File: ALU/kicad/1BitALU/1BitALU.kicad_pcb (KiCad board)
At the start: 2 copper layers, 171.5 x 123.2 mm, 55 parts, among them P1 CONN_6, P2 CONN_2, P3 Power, U1 xor3a, U10 and3a, U11 or2a, U12 and3b, U13 inv3b, U14 and3c, U15 or3a, U16 xor1b, U17 xor1a, U18 xor2b, U19 and4a, U2 and2a, U20 xor2a, U21 and4b, U22 and4c, U23 or3b, U24 and5a, U25 and5b, U26 inv5c, U27 and5c, U28 or3c, U29 and6a, U3 xor3b, U30 inv6b, U31 and6b, U32 inv6c, U33 and6c, U34 or3d, U4 and2b, U5 or1b, U6 and1a, U7 and1b, U8 or1a, U9 or2b

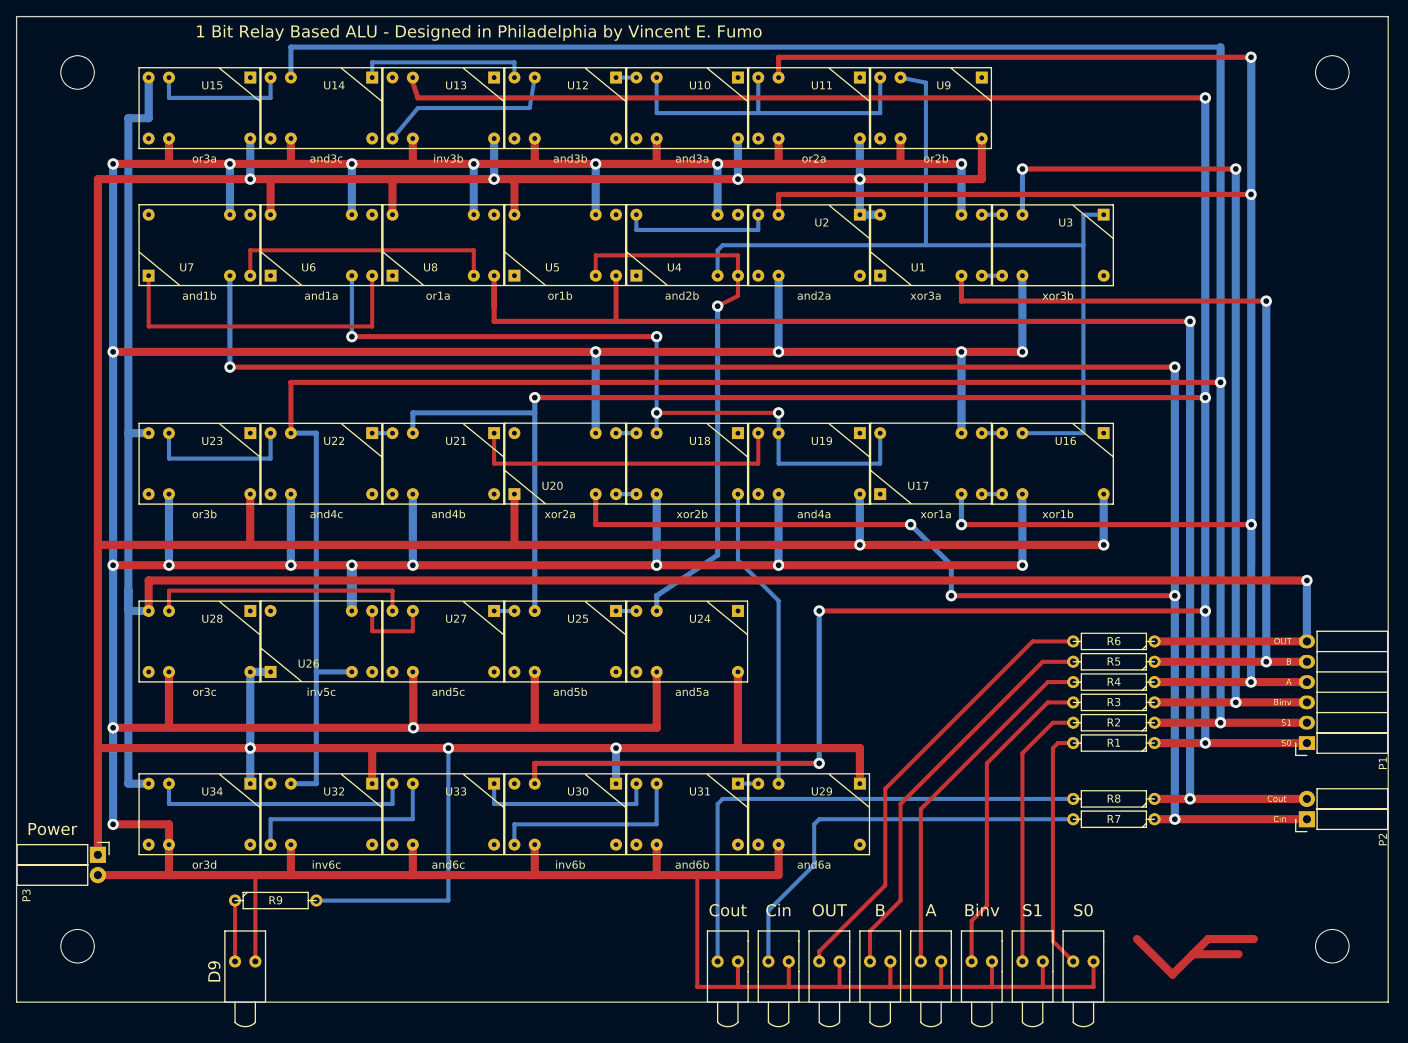
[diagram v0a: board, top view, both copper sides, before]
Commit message: bigger drill holes
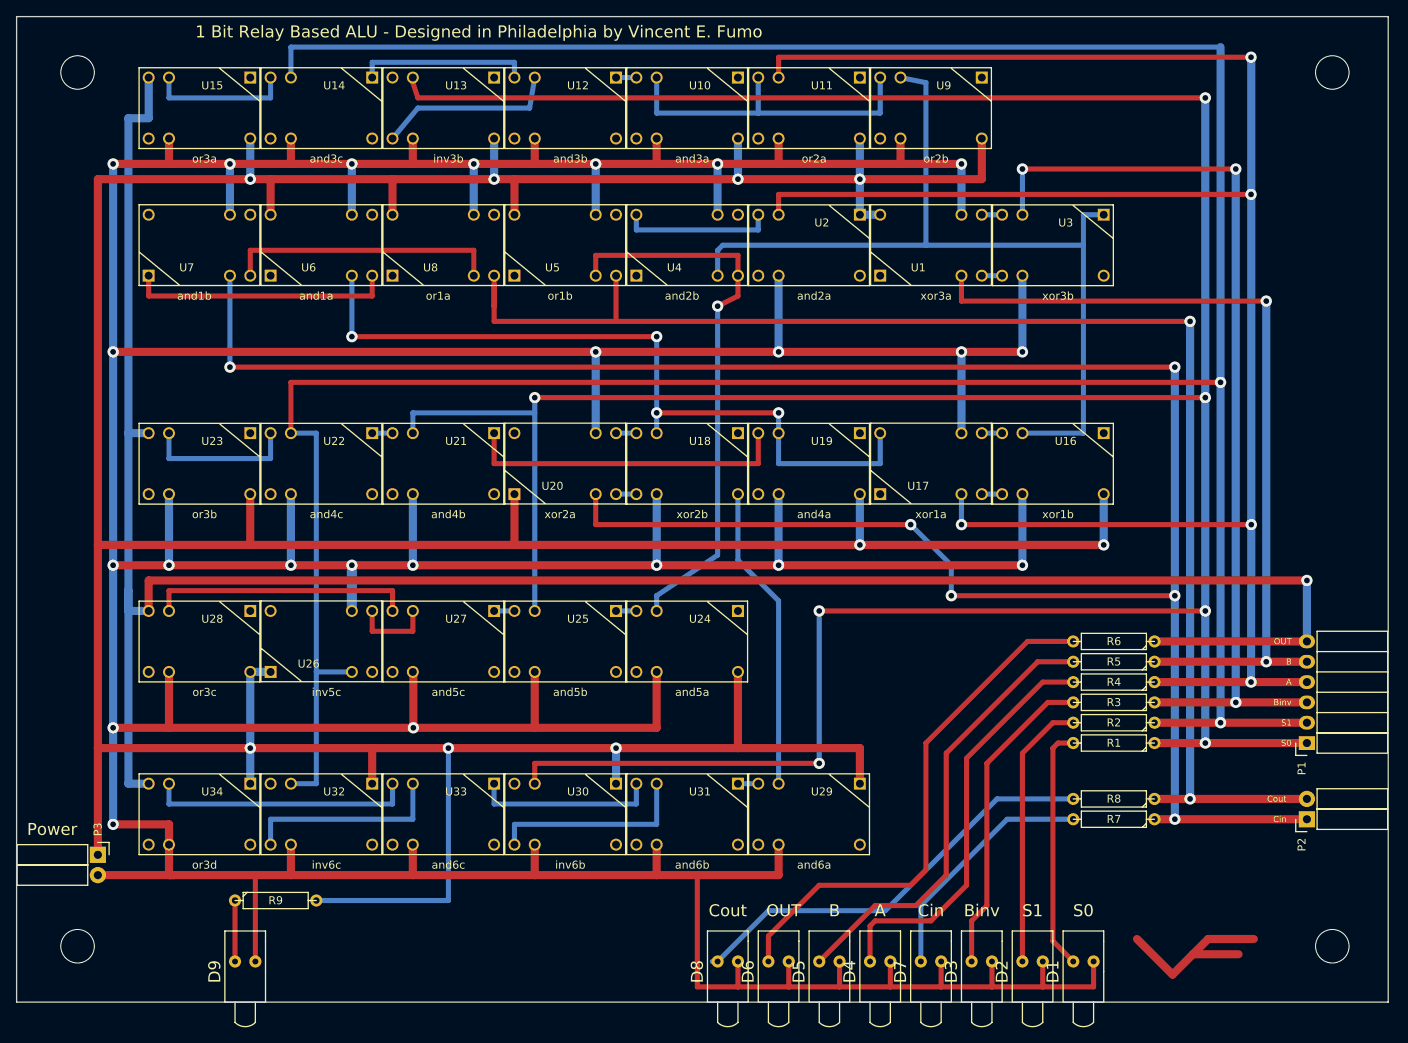
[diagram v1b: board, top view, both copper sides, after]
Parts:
- moved D7 19.1 mm to (164.1, 150.8)
- moved D5 6.35 mm to (151.4, 150.8)
- moved D4 6.35 mm to (157.8, 150.8)
- moved D6 6.35 mm to (145.1, 150.8)
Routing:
- net Net-(D7-Pad1): track 52.2 -> 30.5 mm
- net Net-(D8-Pad1): track 64.4 -> 54.1 mm
- net Net-(D6-Pad1): track 56.1 -> 65.8 mm
- net Net-(U6-Pad6): track 40.6 -> 33.0 mm
- net Net-(D4-Pad1): track 44.7 -> 51.8 mm
- net Net-(D5-Pad1): track 50.2 -> 56.2 mm
